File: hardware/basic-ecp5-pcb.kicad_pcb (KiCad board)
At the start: 4 copper layers, 100 x 68 mm, 76 parts, among them J1 Conn_01x02, J10 Conn_02x05_Odd_Even, J2 Conn_02x20_Odd_Even, J3 Conn_02x06_Odd_Even, J4 Conn_02x06_Odd_Even, J5 Conn_02x06_Odd_Even, J6 Conn_02x06_Odd_Even, J7 Conn_02x06_Odd_Even, J8 Conn_02x06_Odd_Even, J9 Conn_02x20_Odd_Even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

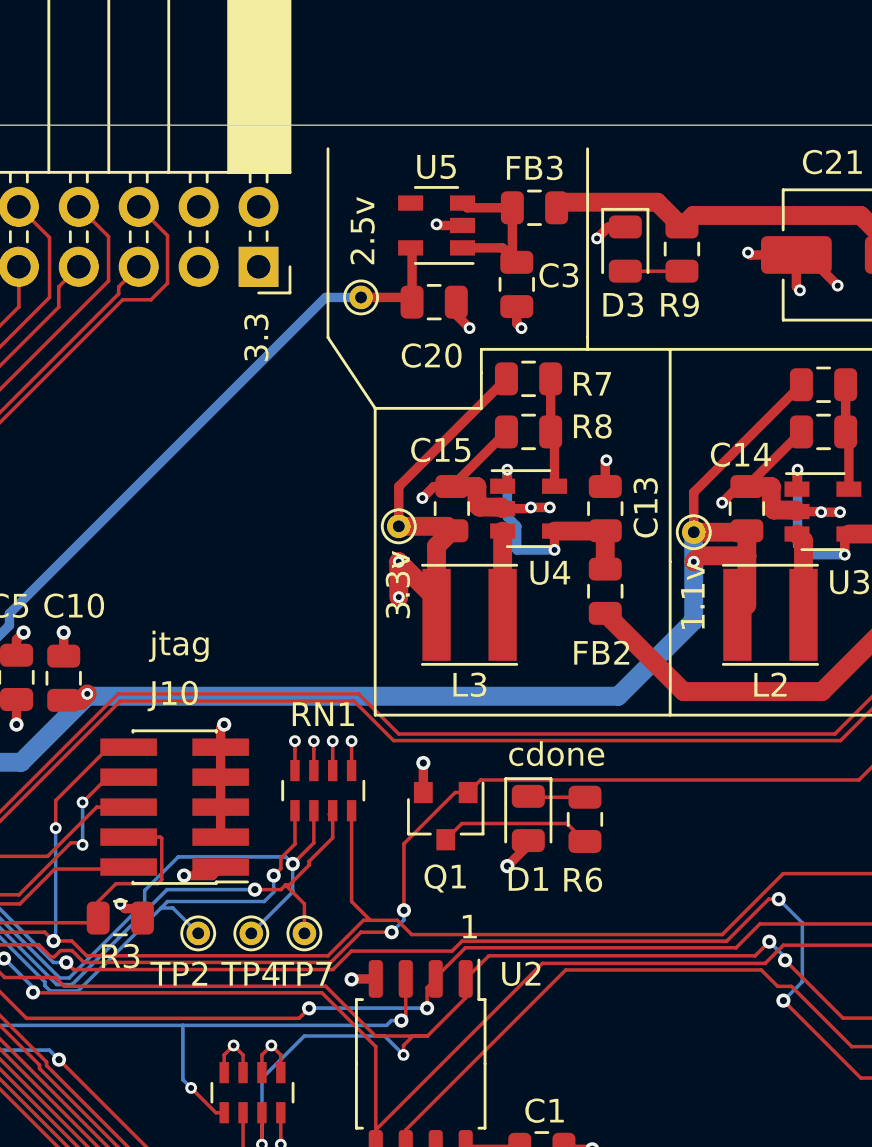
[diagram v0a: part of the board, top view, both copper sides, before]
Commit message: cleanup config silkscreen
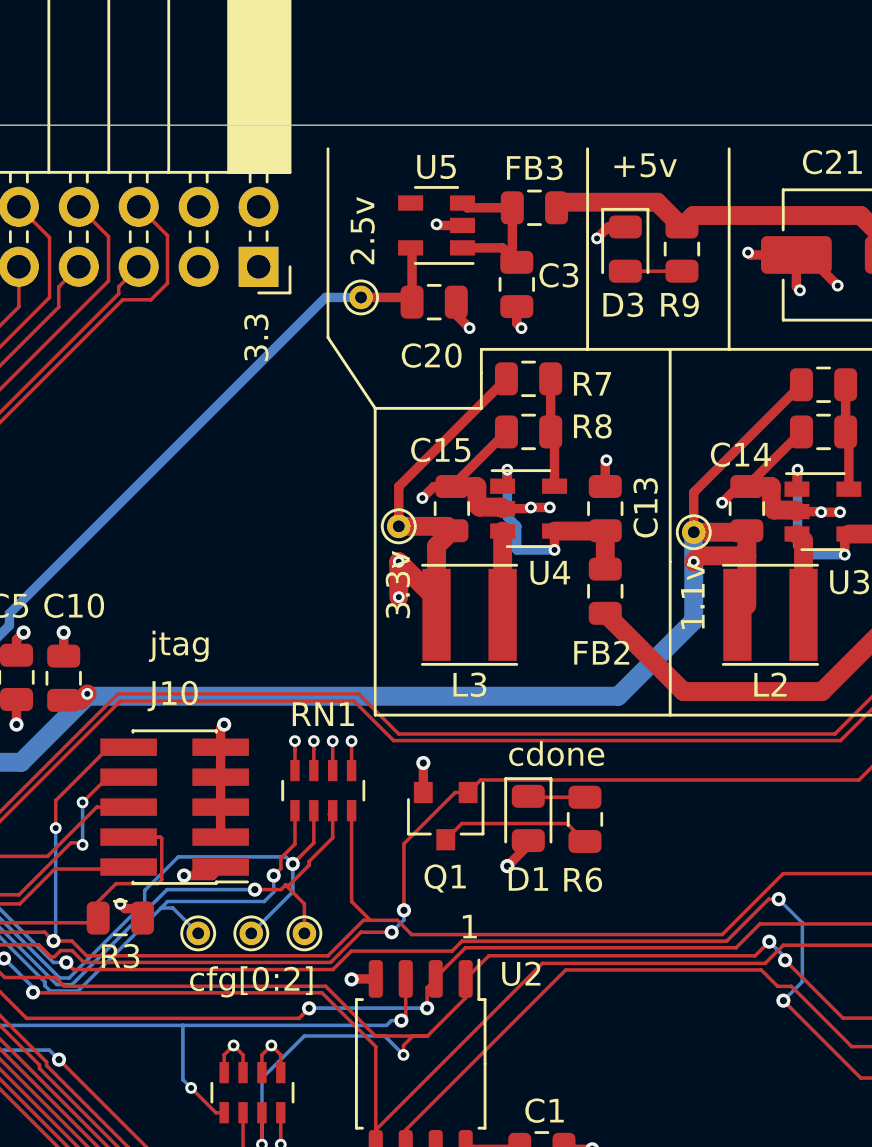
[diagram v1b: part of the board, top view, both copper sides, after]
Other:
- board text added: "cfg[0:2]"

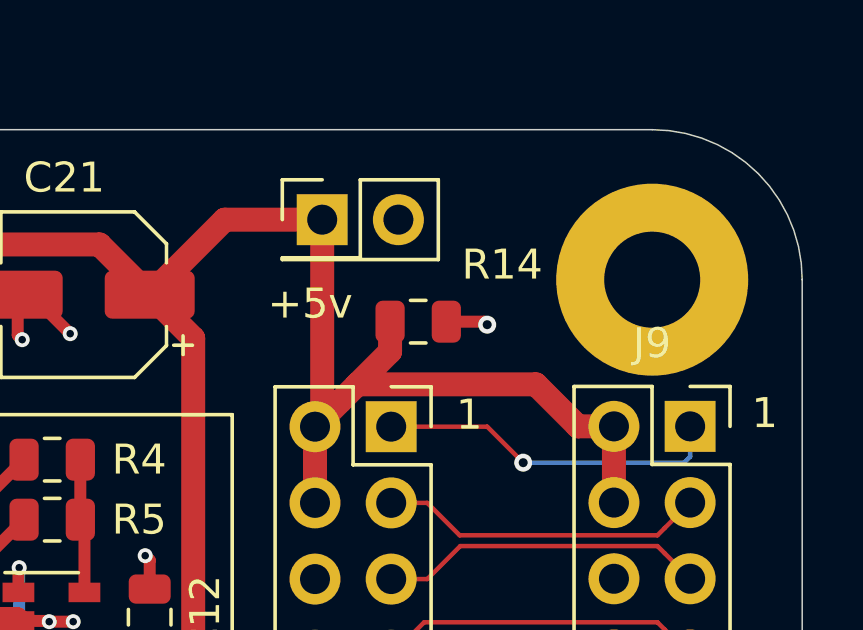
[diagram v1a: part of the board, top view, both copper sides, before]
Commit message: removed unneeded pullup for PG pin on buck converters
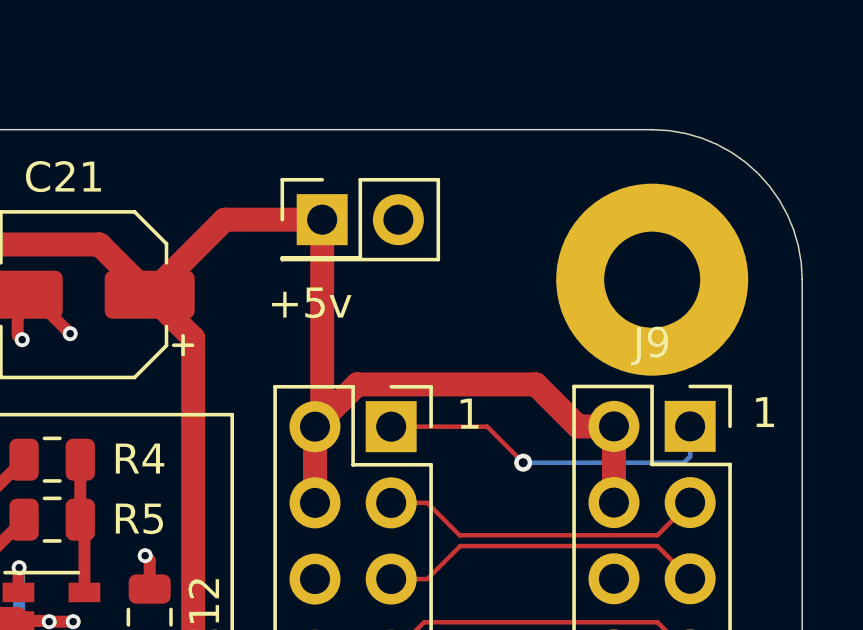
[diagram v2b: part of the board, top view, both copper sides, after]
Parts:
- removed R14: 500k, Resistor_SMD:R_0805_2012Metric
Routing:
- net +5V: track 80.2 -> 77.6 mm
- net GND: track 81.7 -> 80.3 mm, vias 51 -> 50

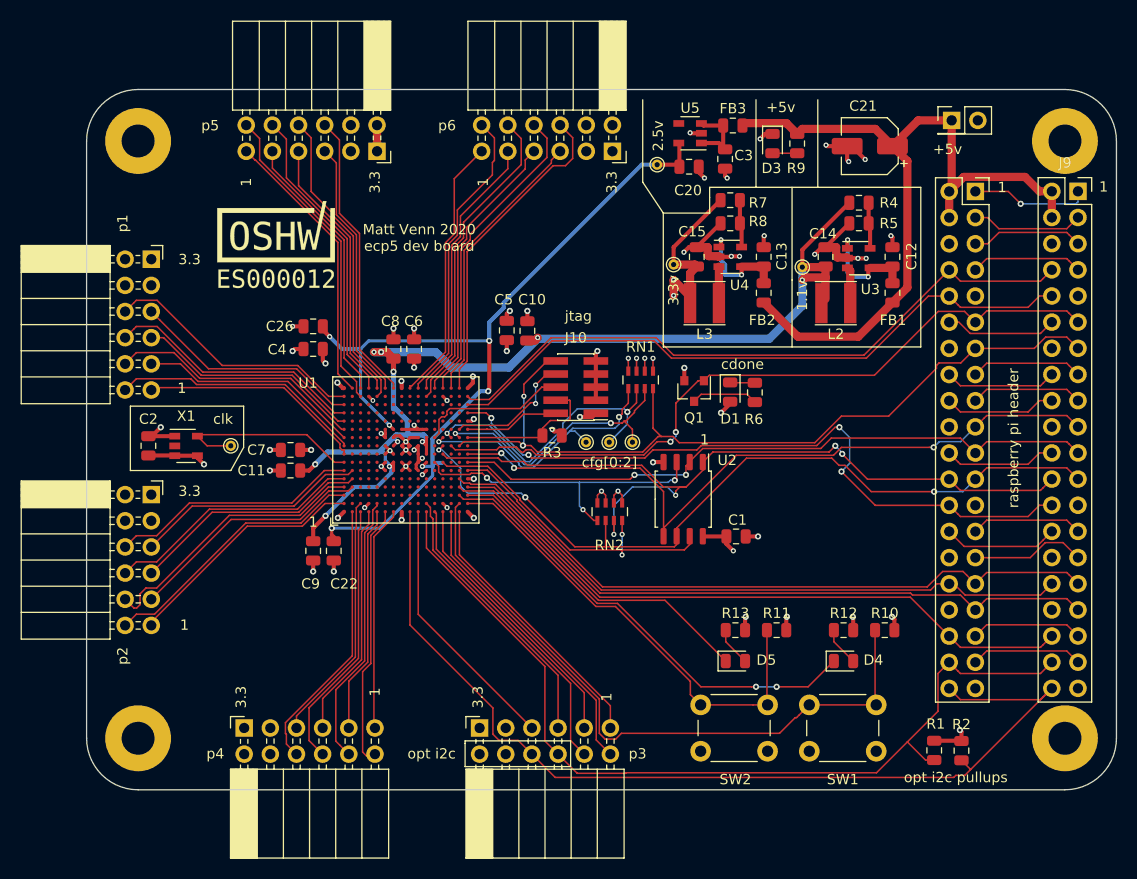
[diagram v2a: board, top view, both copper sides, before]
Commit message: remove a few stubs on copper fpga supply. improve silk
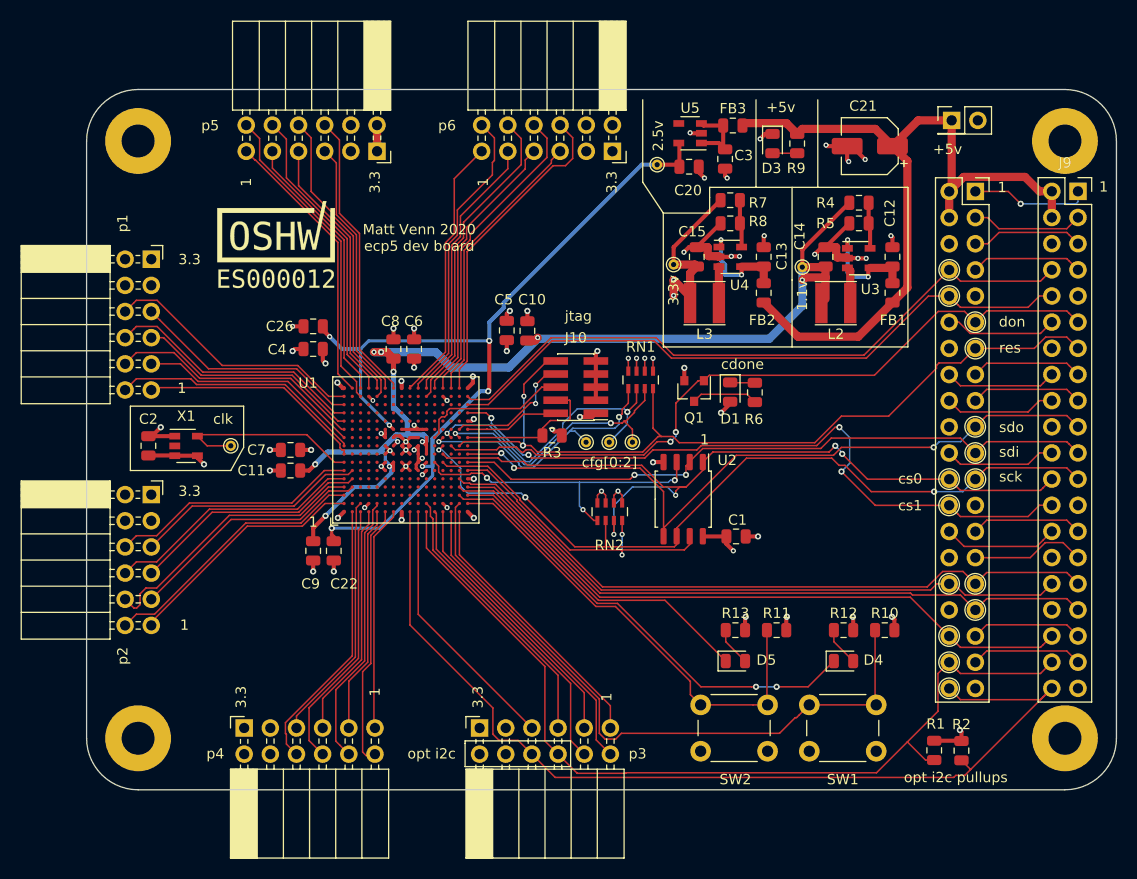
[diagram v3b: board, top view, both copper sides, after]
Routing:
- net +2V5: track 88.2 -> 87.2 mm
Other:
- board text added: "cs0"
- board text added: "cs1"
- board text added: "don"
- board text added: "res"
- board text added: "sck"
- board text added: "sdi"
- board text added: "sdo"
- board text removed: "raspberry pi header"
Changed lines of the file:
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@@
   (general
     (thickness 1.6)
-    (drawings 78)
-    (tracks 1282)
+    (drawings 99)
+    (tracks 1278)
     (zones 0)
     (modules 75)
@@
     (tags capacitor)
     (attr smd)
-    (fp_text reference C14 (at 2.25 -0.25 180) (layer F.SilkS)
+    (fp_text reference C14 (at 2 -2.5 270) (layer F.SilkS)
       (effects (font (size 1 1) (thickness 0.15)))
     )
@@
     (tags resistor)
     (attr smd)
-    (fp_text reference R4 (at -2.9 0) (layer F.SilkS)
+    (fp_text reference R4 (at 3.25 0) (layer F.SilkS)
       (effects (font (size 1 1) (thickness 0.15)))
     )
@@
     (tags capacitor)
     (attr smd)
-    (fp_text reference C12 (at 0.05 1.85 270) (layer F.SilkS)
+    (fp_text reference C12 (at 4.25 -0.25 270) (layer F.SilkS)
       (effects (font (size 1 1) (thickness 0.15)))
     )
@@
     (tags resistor)
     (attr smd)
-    (fp_text reference R5 (at 2.9 0) (layer F.SilkS)
+    (fp_text reference R5 (at -3.25 0) (layer F.SilkS)
       (effects (font (size 1 1) (thickness 0.15)))
     )
@@
     (pad 40 thru_hole oval (at -2.54 48.26) (size 1.7 1.7) (drill 1) (layers *.Cu *.Mask)
       (net 198 p3_10))
-    (model ${KISYS3DMOD}/Connector_PinSocket_2.54mm.3dshapes/PinSocket_2x20_P2.54mm_Vertical.wrl
-      (at (xyz 0 0 0))
-      (scale (xyz 1 1 1))
-      (rotate (xyz 0 0 0))
-    )
   )
   (module Resistor_SMD:R_0805_2012Metric (layer F.Cu)
@@
       (net 240 /fpga/cfg_2))
   )
+  (gr_text don (at 163.58 73.56) (layer F.SilkS)
+    (effects (font (size 1 1) (thickness 0.15)) (justify left))
+  )
+  (gr_text "res\n" (at 163.6 76.09) (layer F.SilkS)
+    (effects (font (size 1 1) (thickness 0.15)) (justify left))
+  )
+  (gr_circle (center 161.29 99) (end 161.89 99.8) (layer F.SilkS) (width 0.12))
+  (gr_circle (center 158.76 68.52) (end 159.36 69.32) (layer F.SilkS) (width 0.12))
+  (gr_circle (center 158.76 71.05) (end 159.36 71.85) (layer F.SilkS) (width 0.12))
+  (gr_circle (center 161.28 73.6) (end 161.88 74.4) (layer F.SilkS) (width 0.12))
+  (gr_circle (center 161.3 76.16) (end 161.9 76.96) (layer F.SilkS) (width 0.12))
+  (gr_circle (center 161.28 83.75) (end 161.88 84.55) (layer F.SilkS) (width 0.12))
+  (gr_circle (center 161.29 86.3) (end 161.89 87.1) (layer F.SilkS) (width 0.12))
+  (gr_circle (center 161.3 88.84) (end 161.9 89.64) (layer F.SilkS) (width 0.12))
+  (gr_circle (center 158.75 91.38) (end 159.35 92.18) (layer F.SilkS) (width 0.12))
+  (gr_circle (center 158.75 88.83) (end 159.35 89.63) (layer F.SilkS) (width 0.12))
+  (gr_circle (center 158.75 109.15) (end 159.35 109.95) (layer F.SilkS) (width 0.12))
+  (gr_circle (center 158.75 104.07) (end 159.35 104.87) (layer F.SilkS) (width 0.12))
+  (gr_circle (center 161.29 101.54) (end 161.89 102.34) (layer F.SilkS) (width 0.12))
+  (gr_circle (center 158.75 106.62) (end 159.35 107.42) (layer F.SilkS) (width 0.12))
+  (gr_circle (center 158.75 99) (end 159.35 99.8) (layer F.SilkS) (width 0.12))
+  (gr_text cs1 (at 153.8 91.4) (layer F.SilkS)
+    (effects (font (size 1 1) (thickness 0.15)) (justify left))
+  )
+  (gr_text sck (at 163.6 88.6) (layer F.SilkS)
+    (effects (font (size 1 1) (thickness 0.15)) (justify left))
+  )
+  (gr_text "sdi\n" (at 163.6 86.2) (layer F.SilkS)
+    (effects (font (size 1 1) (thickness 0.15)) (justify left))
+  )
+  (gr_text "sdo\n" (at 163.6 83.8) (layer F.SilkS)
+    (effects (font (size 1 1) (thickness 0.15)) (justify left))
+  )
+  (gr_text cs0 (at 153.8 88.8) (layer F.SilkS)
+    (effects (font (size 1 1) (thickness 0.15)) (justify left))
+  )
   (gr_line (start 146 60.5) (end 146 52) (layer F.SilkS) (width 0.12))
   (gr_text +5v (at 142.41 52.73) (layer F.SilkS)
@@
   (gr_line (start 90.25 81.75) (end 79.25 81.75) (layer F.SilkS) (width 0.12))
   (gr_line (start 129 60) (end 131 63) (layer F.SilkS) (width 0.12))
-  (gr_line (start 140 60.5) (end 156 60.5) (layer F.SilkS) (width 0.12))
+  (gr_line (start 140 60.5) (end 154.75 60.5) (layer F.SilkS) (width 0.12))
   (gr_text 1.1v (at 144.5 71 90) (layer F.SilkS)
     (effects (font (size 1 1) (thickness 0.15)))
@@
   (gr_line (start 143.5 69.5) (end 143.5 60.5) (layer F.SilkS) (width 0.12))
   (gr_line (start 143.5 76) (end 143.5 69.5) (layer F.SilkS) (width 0.12))
-  (gr_line (start 156 76) (end 156 60.5) (layer F.SilkS) (width 0.12))
-  (gr_line (start 131 76) (end 156 76) (layer F.SilkS) (width 0.12))
+  (gr_line (start 154.75 76) (end 154.75 60.5) (layer F.SilkS) (width 0.12))
+  (gr_line (start 131 76) (end 154.75 76) (layer F.SilkS) (width 0.12))
   (gr_line (start 131 63) (end 131 76) (layer F.SilkS) (width 0.12))
   (gr_line (start 140 60.5) (end 140 52) (layer F.SilkS) (width 0.12))
@@
     (effects (font (size 1 1) (thickness 0.15)))
   )
-  (gr_text "raspberry pi header" (at 165 84.85 90) (layer F.SilkS)
-    (effects (font (size 1 1) (thickness 0.15)))
-  )
   (gr_line (start 170 56) (end 170 114) (layer Dwgs.User) (width 0.15))
   (dimension 58 (width 0.15) (layer Dwgs.User)
@@
   (segment (start 106.2 84.6) (end 107.8 84.6) (width 0.3) (layer B.Cu) (net 157))
   (segment (start 107.8 84.6) (end 107.93999 84.73999) (width 0.4) (layer B.Cu) (net 157))
-  (segment (start 107.93999 84.73999) (end 107.93999 85.208713) (width 0.4) (layer B.Cu) (net 157))
+  (segment (start 108 84.73999) (end 108 85.208713) (width 0.4) (layer B.Cu) (net 157))
   (segment (start 108 86.4) (end 108 85.268723) (width 0.3) (layer F.Cu) (net 157))
   (segment (start 108 84.8) (end 108 85.148703) (width 0.3) (layer F.Cu) (net 157))
@@
   (segment (start 109.6 86.4) (end 109.985001 86.785001) (width 0.15) (layer F.Cu) (net 163))
   (segment (start 117.450834 87.119989) (end 117.820867 87.490022) (width 0.15) (layer F.Cu) (net 163))
-  (segment (start 108.733236 87.266764) (end 109.310038 87.266764) (width 0.4) (layer B.Cu) (net 164))
   (via (at 98.8 93.6) (size 0.6) (drill 0.3) (layers F.Cu B.Cu) (net 164))
   (segment (start 98.8 94.6625) (end 99 94.8625) (width 0.3) (layer F.Cu) (net 164))
   (segment (start 98.8 93.6) (end 98.8 94.2625) (width 0.3) (layer F.Cu) (net 164))
-  (segment (start 109.310038 87.266764) (end 109.530041 87.266764) (width 0.4) (layer B.Cu) (net 164))
   (segment (start 99 94.4625) (end 98.8 94.2625) (width 0.4) (layer F.Cu) (net 164))
   (segment (start 99 94.8625) (end 99 94.4625) (width 0.4) (layer F.Cu) (net 164))
@@
   (via (at 104.4 83.6) (size 0.5) (drill 0.25) (layers F.Cu B.Cu) (net 164))
   (segment (start 104.8 84) (end 104.4 83.6) (width 0.3) (layer F.Cu) (net 164))
-  (segment (start 108.589999 87.589999) (end 108.6 87.6) (width 0.4) (layer B.Cu) (net 164))
-  (segment (start 108.6 87.4) (end 108.733236 87.266764) (width 0.3) (layer B.Cu) (net 164))
   (segment (start 108.6 88.500001) (end 108.6 87.4) (width 0.3) (layer B.Cu) (net 164))
   (segment (start 98.8 93.6) (end 103.500001 93.6) (width 0.3) (layer B.Cu) (net 164))

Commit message: * Add missing qspi to the Pi to be able to program bitstream faster. Done
* used IS25LP016D-JBLE as flash, but
 it has problems with enabling QE for QSPI.
Relace with the model used on icebreaker
This is already done, comment should be removed

* ecp5 SPI clock pin can't be used as an input
 so have to [add a bodge wire](https://github.com/mattvenn/basic-ecp5-pcb/issues/3)
for SPI peripheral comms with Pi.
See the test-spi-clk-in branch for a workaround.
Worked around by connecting this pin to a second FPGA pin

* connected I2C pins are just GPIOs. I have found the Pi's I2C hardware unusable, so always use the slower bitbanged version.
Connected I2C pins to official pins.
Removed pull resistors as this is not needed
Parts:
- removed R1, R2: 10k, Resistor_SMD:R_0805_2012Metric
- U2: value IS25LP016D-JBLE -> W25Q128JVSIM
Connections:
- J2 pad 18: /gp24 -> sd_io2
- J2 pad 22: /gp25 -> sd_io3
- J2 pad 3: /gp2 -> p3_9
- J2 pad 38: p3_9 -> /gp20
- J2 pad 40: p3_10 -> /gp21
- J2 pad 5: /gp3 -> p3_10
- J9 pad 18: /gp24 -> sd_io2
- J9 pad 22: /gp25 -> sd_io3
- J9 pad 3: /gp2 -> p3_9
- J9 pad 38: p3_9 -> /gp20
- J9 pad 40: p3_10 -> /gp21
- J9 pad 5: /gp3 -> p3_10
- U1 pad M5: Net-(U1-PadM5) -> sd_clk
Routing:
- net p3_9: track 88.4 -> 146.9 mm
- net sd_io2: track 31.1 -> 71.8 mm
- net sd_io3: track 32.5 -> 72.4 mm, vias 2 -> 4
- net p3_10: track 96.7 -> 133.1 mm, vias 0 -> 1
- net /gp24: track 10.9 -> 0.00 mm
- net /gp20: track 0.00 -> 10.9 mm
- net /gp25: track 10.9 -> 0.00 mm
- net /gp21: track 0.00 -> 10.9 mm
- net /gp3: track 10.9 -> 0.00 mm
- net /gp2: track 10.9 -> 0.00 mm
- net +3.3VP: track 64.0 -> 60.2 mm, vias 24 -> 23
- net sd_clk: track 77.3 -> 80.9 mm
